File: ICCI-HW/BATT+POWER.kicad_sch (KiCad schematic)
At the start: 61 parts, among them SW601 SW_SPDT, U601 NCV8164ASN180T1G, U602 AP62301WU-7, U603 MAX77960BEFV12+

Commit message: hw: updates
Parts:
- removed NT601: NetTie_2, NetTie:NetTie-2_SMD_Pad2.0mm, symbol Device:NetTie_2
- L601: footprint Inductor_SMD:L_Bourns_SRP7028A_7.3x6.6mm -> ICCI-LIB:ICCI_L_Bourns_SRP7028A_7.3x6.6mm
- L602: footprint Inductor_SMD:L_Coilcraft_XxL4040 -> ICCI-LIB:ICCI_L_Coilcraft_XxL4040
- R621: value 22.6k -> 54.9k
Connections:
- net BATSP is gone; now on net +BATT: U603.11 (BATSP)
- net +3V3: now also R602.1; no longer D601.2 (A)
- net ~{BATT_S_LED}: now also D601.1 (K); no longer R602.2
- net BST2: now reaches C615.1, U603.9 (BST2)
- net LX2: now reaches C615.2, L602.2, U603.5 (LX2)
- net BST1: now reaches C614.1, U603.1 (BST1)
- net LX1: now reaches C614.2, L602.1, U603.3 (LX1)
- new net: D601.2 (A), R602.2
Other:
- note added: "1.5A Input max"
- note added: "According to the DS of CP2102N, implementing USB BC 1.2, 1.5A is the TOTAL MAX CURRENT drawn from USB 5V rail."
- note added: "On/Off Switch. OBV battery rail remains active."
- note added: "PGND"
- note added: "SGND"
- note added: "The regulator always priorities the system, the remaining power will be delivered to battery if charging. So, if charging at 1.5A and system is using 1A, battery charger will get only 0.5A. If Input power is not enough to power the system, battery will output current to system. So, if available input power is 0.5A and system is using 1A, if battery are charged they will deliver the remaining 0.5A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"
- note added: "There are also some proprietary protocols (e.g. Apple, Samsung and Blackberry chargers) that allows to draw more than 1.5A without USB C PD, but they are not implemented on CP2102N."
- note added: "USB BC 1.2 Imax = 1.5A."
- note removed: "2.5A Input max"
- note removed: "Analog GND"
- note removed: "Check if USB BC is max 1.5A. From USB BC 1.2 Specs seems that I>1.5A are allowed."
- note removed: "If batteries The regulator always priorities the system, the remaining power will be delivered to battery if charging. So, if charging at 1.5A and system is using 1A, battery charger will get only 0.5A. If Input power is not enough to power the system, battery will output current to system. So, if available input power is 0.5A and system is using 1A, if battery are charged they will deliver the r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"
- note removed: "Power GND"
- company: tollsimy -> Simone Tollardo
- moved on the sheet: C601, C602, C603, C608, C610, C612, C614, C615, C618, D601, D602, D603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

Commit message: hw: updates
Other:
- moved on the sheet: C616, C617, C618, C619

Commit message: start layout
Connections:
- net +BATT: no longer D605.2 (A)
- net VCC: no longer D605.1 (K)
- net B1-B2: now reaches BT601.C1+, BT601.C2-
- new net BATT: D605.2 (A)
- new net SYS: D605.1 (K)
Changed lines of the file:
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@@
     (company "Simone Tollardo")
   )
+  (junction (at 26.035 66.04) (diameter 0) (color 0 0 0 0)
+  )
   (junction (at 65.405 135.89) (diameter 0) (color 0 0 0 0)
   )
@@
     (stroke (width 0) (type default) (color 0 0 0 0))
   )
+  (wire (pts (xy 17.145 66.04) (xy 26.035 66.04))
+    (stroke (width 0) (type default) (color 0 0 0 0))
+  )
   (wire (pts (xy 158.75 101.6) (xy 158.75 100.33))
     (stroke (width 0) (type default) (color 0 0 0 0))
@@
     (stroke (width 0) (type default) (color 0 0 0 0))
   )
-  (wire (pts (xy 26.035 65.405) (xy 26.035 66.675))
+  (wire (pts (xy 26.035 65.405) (xy 26.035 66.04))
     (stroke (width 0) (type default) (color 0 0 0 0))
   )
@@
   )
   (wire (pts (xy 31.75 170.18) (xy 42.545 170.18))
+    (stroke (width 0) (type default) (color 0 0 0 0))
+  )
+  (wire (pts (xy 26.035 66.04) (xy 26.035 66.675))
     (stroke (width 0) (type default) (color 0 0 0 0))
   )
@@
     (effects (font (size 1.27 1.27)) (justify left bottom))
   )
-  (label "BATT" (at 44.45 54.61 180)
+  (label "+BATT" (at 44.45 54.61 180)
     (effects (font (size 1.27 1.27)) (justify right bottom))
   )
@@
     (effects (font (size 1.27 1.27)) (justify left bottom))
   )
+  (label "B1-B2" (at 17.145 66.04 0)
+    (effects (font (size 1.27 1.27)) (justify left bottom))
+  )
   (label "SW_BST" (at 111.76 143.51 0)
     (effects (font (size 1.27 1.27)) (justify left bottom))
@@
     (effects (font (size 1.27 1.27)) (justify left bottom))
   )
-  (label "BATT" (at 201.295 68.58 180)
+  (label "+BATT" (at 201.295 68.58 180)
     (effects (font (size 1.27 1.27)) (justify right bottom))
   )
@@
     (effects (font (size 1.27 1.27)) (justify left bottom))
   )
-  (label "SYS" (at 200.025 53.34 180)
-    (effects (font (size 1.27 1.27)) (justify right bottom))
-  )
+  (label "VSYS" (at 201.295 53.34 180)
+    (effects (font (size 1.27 1.27)) (justify right bottom))
+  )

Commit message: layout updates
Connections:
- net BATT is gone; now on net +BATT: D605.2 (A)
- net SYS is gone; now on net VCC: D605.1 (K)
- net EN: now reaches SW601.2 (B), U602.5 (EN)
- net FUSE_OUT: now reaches D602.1 (A1), D603.2 (A), F601.1
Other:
- note added: "Needed only if AS7341 used."
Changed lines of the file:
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@@
+    (effects (font (size 1.27 1.27)) (justify left bottom))
+  )
+  (text "Needed only if AS7341 used." (at 37.465 162.56 0)
     (effects (font (size 1.27 1.27)) (justify left bottom))
   )
@@
     (effects (font (size 1.27 1.27)) (justify left bottom))
   )
-  (text "1V8 Linear" (at 40.005 163.195 0)
+  (text "1V8 Linear" (at 39.37 160.655 0)
     (effects (font (size 3 3) (thickness 0.6) bold) (justify left bottom))
   )
@@
     (effects (font (size 1.27 1.27)) (justify left bottom))
   )
+  (label "EN" (at 90.17 140.97 180)
+    (effects (font (size 1.27 1.27)) (justify right bottom))
+  )
   (label "+BATT" (at 44.45 54.61 180)
     (effects (font (size 1.27 1.27)) (justify right bottom))
@@
     (effects (font (size 1.27 1.27)) (justify right bottom))
   )
-  (label "BATT" (at 252.095 39.37 0)
-    (effects (font (size 1.27 1.27)) (justify left bottom))
-  )
-  (label "SYS" (at 273.685 39.37 180)
+  (label "+BATT" (at 252.095 39.37 0)
+    (effects (font (size 1.27 1.27)) (justify left bottom))
+  )
+  (label "VSYS" (at 273.685 39.37 180)
     (effects (font (size 1.27 1.27)) (justify right bottom))
   )
@@
     (effects (font (size 1.27 1.27)) (justify left bottom))
   )
+  (label "FUSE_OUT" (at 53.34 135.89 180)
+    (effects (font (size 1.27 1.27)) (justify right bottom))
+  )
   (label "SDA1" (at 74.93 53.34 180)

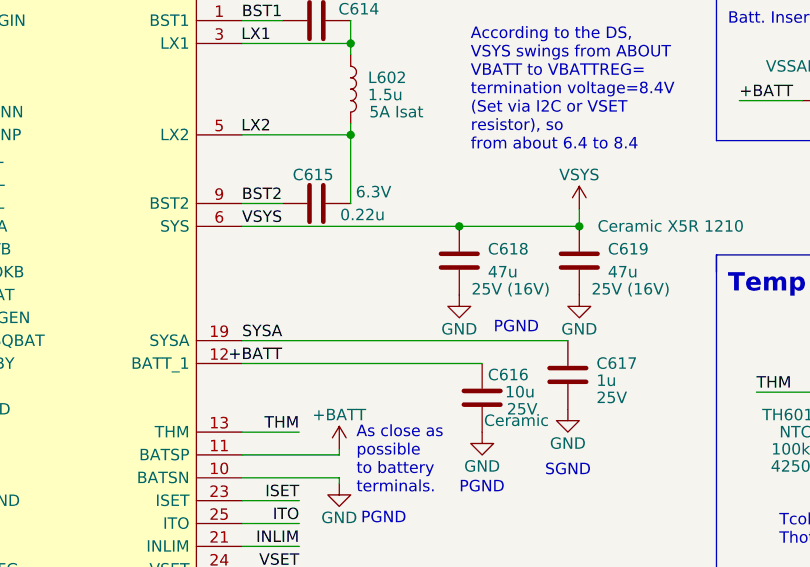
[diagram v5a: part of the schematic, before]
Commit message: hw: fix missing contact from SYS to SYSA on MAX77960
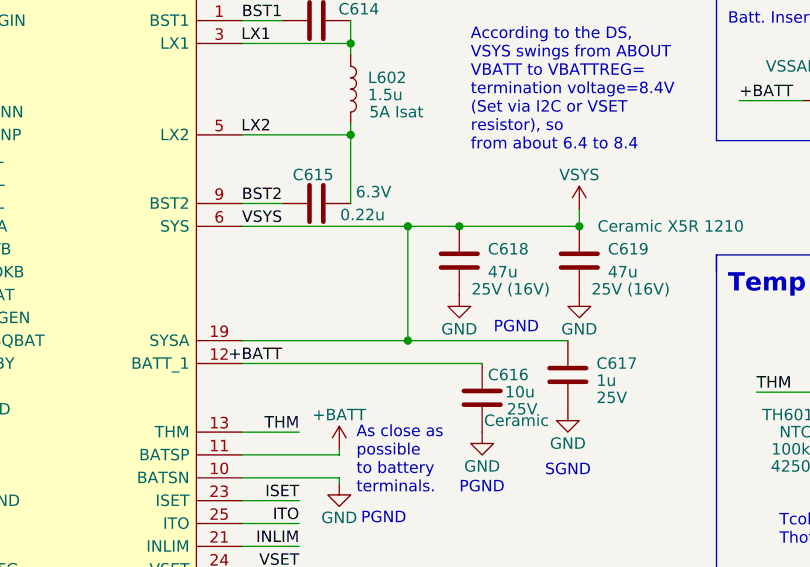
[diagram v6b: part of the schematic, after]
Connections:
- net SYSA is gone; now on net VCC: C617.1, U603.19 (SYSA)
